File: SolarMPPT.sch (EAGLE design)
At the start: 33 parts, among them J1 CORTEX_DEBUG_SMD, U1 STM32F091CCT6, U3 LTC1155, U4 LM22674MRX-5.0, U5 3.3V

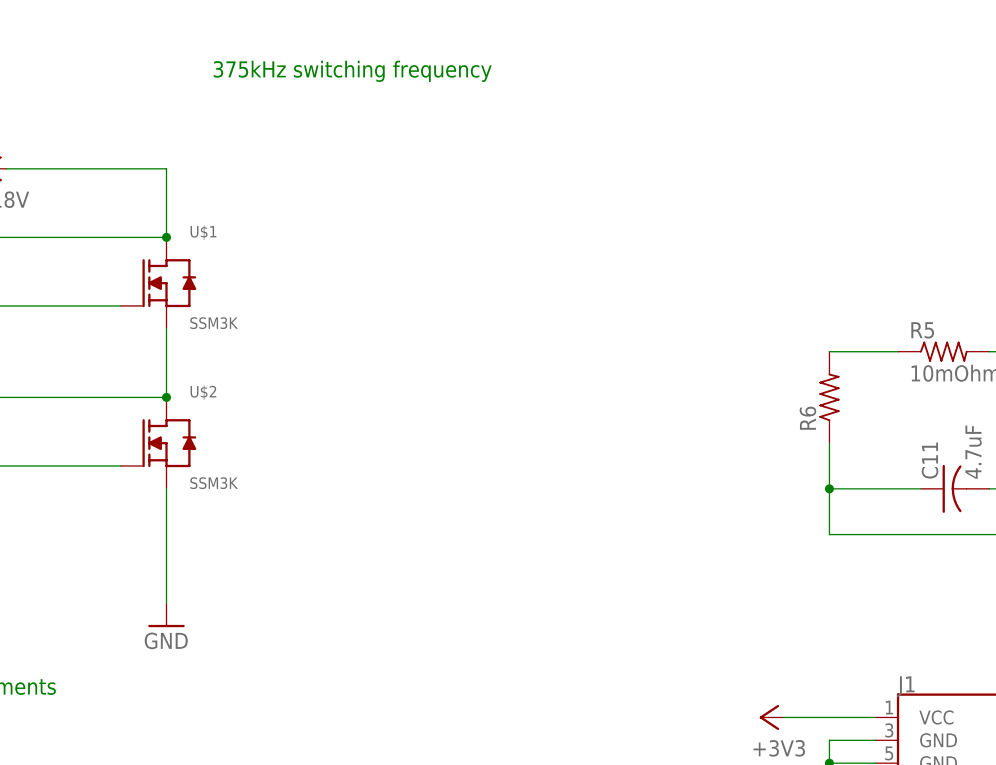
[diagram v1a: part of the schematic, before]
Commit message: finished Buck component selection
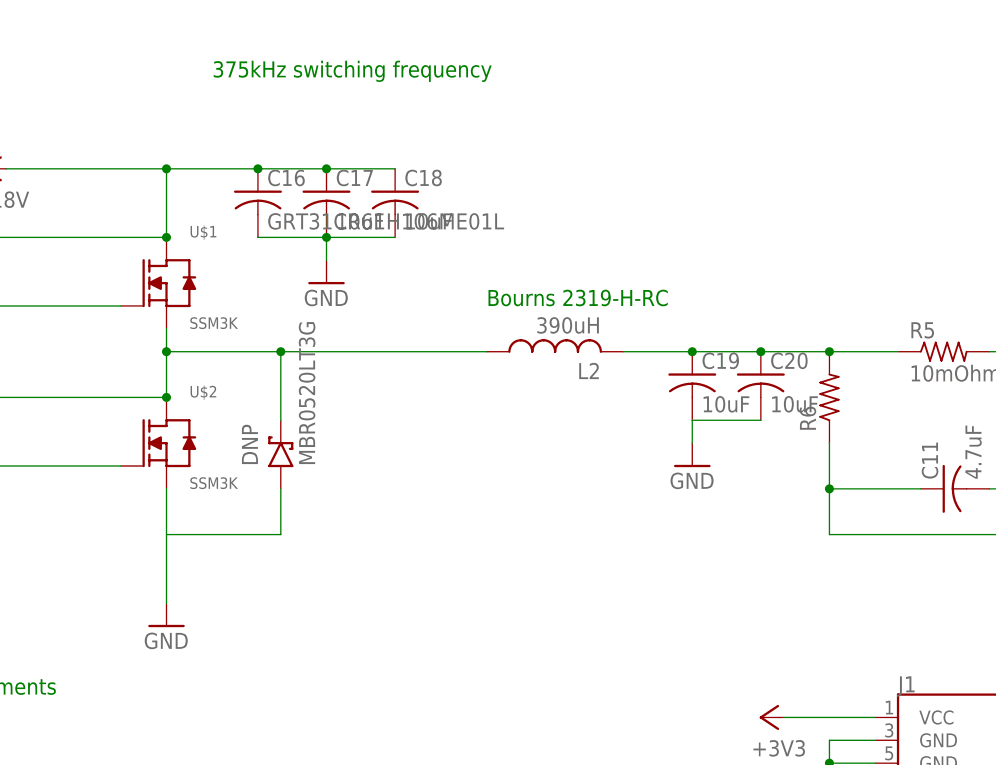
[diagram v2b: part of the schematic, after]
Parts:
- added C16: GRT31CR61H106ME01L, rcl:C-USC1206
- added C17, C18, C19, C20: 10uF, rcl:C-USC1206
- added DNP: MBR0520LT3G, FormE:MBR0520LT3G
- added L2: 390uH, rcl:L-USTJ6-U2
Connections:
- removed net N$3: R5.1, R6.2
- new net N$10: C19.1, C20.1, L2.2, R5.1, R6.2
- net +18V: now also C16.1, C17.1, C18.1
- net GND: now also C16.2, C17.2, C18.2, C19.2, C20.2, DNP.A
- net N$7: now also DNP.K, L2.1
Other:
- note added: "Bourns 2319-H-RC"
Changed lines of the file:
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@@
 <part name="GND16" library="supply1" library_urn="urn:adsk.eagle:library:371" deviceset="GND" device=""/>
 <part name="GND18" library="supply1" library_urn="urn:adsk.eagle:library:371" deviceset="GND" device=""/>
+<part name="C16" library="rcl" library_urn="urn:adsk.eagle:library:334" deviceset="C-US" device="C1206" package3d_urn="urn:adsk.eagle:package:23618/2" value="GRT31CR61H106ME01L"/>
+<part name="C17" library="rcl" library_urn="urn:adsk.eagle:library:334" deviceset="C-US" device="C1206" package3d_urn="urn:adsk.eagle:package:23618/2" value="10uF"/>
+<part name="C18" library="rcl" library_urn="urn:adsk.eagle:library:334" deviceset="C-US" device="C1206" package3d_urn="urn:adsk.eagle:package:23618/2" value="10uF"/>
+<part name="C19" library="rcl" library_urn="urn:adsk.eagle:library:334" deviceset="C-US" device="C1206" package3d_urn="urn:adsk.eagle:package:23618/2" value="10uF"/>
+<part name="C20" library="rcl" library_urn="urn:adsk.eagle:library:334" deviceset="C-US" device="C1206" package3d_urn="urn:adsk.eagle:package:23618/2" value="10uF"/>
+<part name="L2" library="rcl" library_urn="urn:adsk.eagle:library:334" deviceset="L-US" device="TJ6-U2" package3d_urn="urn:adsk.eagle:package:23510/1" value="390uH"/>
+<part name="GND19" library="supply1" library_urn="urn:adsk.eagle:library:371" deviceset="GND" device=""/>
+<part name="GND21" library="supply1" library_urn="urn:adsk.eagle:library:371" deviceset="GND" device=""/>
+<part name="DNP" library="FormE" deviceset="MBR0520LT3G" device="" value="MBR0520LT3G"/>
 </parts>
 <sheets>
@@
 <text x="-73.66" y="228.6" size="1.778" layer="97" rot="MR0">NC</text>
 <text x="-187.96" y="129.54" size="1.778" layer="91">Use LT1255 for higher voltage requirements</text>
+<text x="-91.44" y="172.72" size="1.778" layer="91">Bourns 2319-H-RC</text>
 </plain>
 <instances>
@@
 <instance part="GND18" gate="1" x="-203.2" y="147.32" smashed="yes">
 <attribute name="VALUE" x="-205.74" y="144.78" size="1.778" layer="96"/>
+</instance>
+<instance part="C16" gate="G$1" x="-116.84" y="185.42" smashed="yes">
+<attribute name="NAME" x="-115.824" y="186.055" size="1.778" layer="95"/>
+<attribute name="VALUE" x="-115.824" y="181.229" size="1.778" layer="96"/>
+</instance>
+<instance part="C17" gate="G$1" x="-109.22" y="185.42" smashed="yes">
+<attribute name="NAME" x="-108.204" y="186.055" size="1.778" layer="95"/>
+<attribute name="VALUE" x="-108.204" y="181.229" size="1.778" layer="96"/>
+</instance>
+<instance part="C18" gate="G$1" x="-101.6" y="185.42" smashed="yes">
+<attribute name="NAME" x="-100.584" y="186.055" size="1.778" layer="95"/>
+<attribute name="VALUE" x="-100.584" y="181.229" size="1.778" layer="96"/>
+</instance>
+<instance part="C19" gate="G$1" x="-68.58" y="165.1" smashed="yes">
+<attribute name="NAME" x="-67.564" y="165.735" size="1.778" layer="95"/>
+<attribute name="VALUE" x="-67.564" y="160.909" size="1.778" layer="96"/>
+</instance>
+<instance part="C20" gate="G$1" x="-60.96" y="165.1" smashed="yes">
+<attribute name="NAME" x="-59.944" y="165.735" size="1.778" layer="95"/>
+<attribute name="VALUE" x="-59.944" y="160.909" size="1.778" layer="96"/>
+</instance>
+<instance part="L2" gate="G$1" x="-83.82" y="167.64" smashed="yes" rot="R90">
+<attribute name="NAME" x="-78.74" y="166.37" size="1.778" layer="95" rot="R180"/>
+<attribute name="VALUE" x="-78.74" y="171.45" size="1.778" layer="96" rot="R180"/>
+</instance>
+<instance part="GND19" gate="1" x="-109.22" y="175.26" smashed="yes">
+<attribute name="VALUE" x="-111.76" y="172.72" size="1.778" layer="96"/>
+</instance>
+<instance part="GND21" gate="1" x="-68.58" y="154.94" smashed="yes">
+<attribute name="VALUE" x="-71.12" y="152.4" size="1.778" layer="96"/>
+</instance>
+<instance part="DNP" gate="G$1" x="-114.3" y="157.48" smashed="yes" rot="R90">
+<attribute name="NAME" x="-116.84" y="154.94" size="1.778" layer="95" rot="R90"/>
+<attribute name="VALUE" x="-110.49" y="154.94" size="1.778" layer="96" rot="R90"/>
 </instance>
 </instances>
@@
 <pinref part="U$2" gate="G$1" pin="S"/>
 <pinref part="GND16" gate="1" pin="GND"/>
-<wire x1="-127" y1="152.4" x2="-127" y2="139.7" width="0.1524" layer="91"/>
+<wire x1="-127" y1="152.4" x2="-127" y2="147.32" width="0.1524" layer="91"/>
+<wire x1="-127" y1="147.32" x2="-127" y2="139.7" width="0.1524" layer="91"/>
+<wire x1="-127" y1="147.32" x2="-114.3" y2="147.32" width="0.1524" layer="91"/>
+<pinref part="DNP" gate="G$1" pin="A"/>
+<wire x1="-114.3" y1="147.32" x2="-114.3" y2="152.4" width="0.1524" layer="91"/>
 </segment>
 <segment>
 <pinref part="U3" gate="P" pin="GND"/>
 <pinref part="GND18" gate="1" pin="GND"/>
+</segment>
+<segment>
+<pinref part="C19" gate="G$1" pin="2"/>
+<pinref part="GND21" gate="1" pin="GND"/>
+<pinref part="C20" gate="G$1" pin="2"/>
+<wire x1="-68.58" y1="160.02" x2="-68.58" y2="157.48" width="0.1524" layer="91"/>
+<wire x1="-68.58" y1="160.02" x2="-60.96" y2="160.02" width="0.1524" layer="91"/>
+</segment>
+<segment>
+<pinref part="C16" gate="G$1" pin="2"/>
+<pinref part="C17" gate="G$1" pin="2"/>
+<wire x1="-116.84" y1="180.34" x2="-109.22" y2="180.34" width="0.1524" layer="91"/>
+<pinref part="C18" gate="G$1" pin="2"/>
+<wire x1="-109.22" y1="180.34" x2="-101.6" y2="180.34" width="0.1524" layer="91"/>
+<junction x="-109.22" y="180.34"/>
+<pinref part="GND19" gate="1" pin="GND"/>
+<wire x1="-109.22" y1="177.8" x2="-109.22" y2="180.34" width="0.1524" layer="91"/>
 </segment>
 </net>
@@
 <wire x1="-203.2" y1="180.34" x2="-172.72" y2="180.34" width="0.1524" layer="91"/>
 <junction x="-172.72" y="180.34"/>
+<pinref part="C16" gate="G$1" pin="1"/>
+<wire x1="-127" y1="187.96" x2="-116.84" y2="187.96" width="0.1524" layer="91"/>
+<junction x="-127" y="187.96"/>
+<pinref part="C17" gate="G$1" pin="1"/>
+<wire x1="-116.84" y1="187.96" x2="-109.22" y2="187.96" width="0.1524" layer="91"/>
+<junction x="-116.84" y="187.96"/>
+<pinref part="C18" gate="G$1" pin="1"/>
+<wire x1="-109.22" y1="187.96" x2="-101.6" y2="187.96" width="0.1524" layer="91"/>
+<junction x="-109.22" y="187.96"/>
 </segment>
 </net>
@@
 <wire x1="33.02" y1="30.48" x2="33.02" y2="17.78" width="0.1524" layer="91"/>
 <label x="33.02" y="17.78" size="1.778" layer="95" rot="R90"/>
-</segment>
-</net>
-<net name="N$3" class="0">
-<segment>
-<pinref part="R6" gate="G$1" pin="2"/>
-<pinref part="R5" gate="G$1" pin="1"/>
-<wire x1="-53.34" y1="167.64" x2="-45.72" y2="167.64" width="0.1524" layer="91"/>
 </segment>
 </net>
@@
 <pinref part="U$1" gate="G$1" pin="S"/>
 <pinref part="U$2" gate="G$1" pin="D"/>
-<wire x1="-127" y1="170.18" x2="-127" y2="162.56" width="0.1524" layer="91"/>
+<wire x1="-127" y1="170.18" x2="-127" y2="167.64" width="0.1524" layer="91"/>
 <pinref part="U3" gate="B" pin="D"/>
+<wire x1="-127" y1="167.64" x2="-127" y2="162.56" width="0.1524" layer="91"/>
 <wire x1="-172.72" y1="157.48" x2="-172.72" y2="162.56" width="0.1524" layer="91"/>
 <wire x1="-172.72" y1="162.56" x2="-127" y2="162.56" width="0.1524" layer="91"/>
 <junction x="-127" y="162.56"/>
+<pinref part="L2" gate="G$1" pin="1"/>
+<wire x1="-127" y1="167.64" x2="-114.3" y2="167.64" width="0.1524" layer="91"/>
+<junction x="-127" y="167.64"/>
+<pinref part="DNP" gate="G$1" pin="K"/>
+<wire x1="-114.3" y1="167.64" x2="-91.44" y2="167.64" width="0.1524" layer="91"/>
+<wire x1="-114.3" y1="160.02" x2="-114.3" y2="167.64" width="0.1524" layer="91"/>
+<junction x="-114.3" y="167.64"/>
 </segment>
 </net>
@@
 </segment>
 </net>
+<net name="N$10" class="0">
+<segment>
+<pinref part="L2" gate="G$1" pin="2"/>
+<pinref part="C19" gate="G$1" pin="1"/>
+<wire x1="-76.2" y1="167.64" x2="-68.58" y2="167.64" width="0.1524" layer="91"/>
+<pinref part="C20" gate="G$1" pin="1"/>
+<wire x1="-68.58" y1="167.64" x2="-60.96" y2="167.64" width="0.1524" layer="91"/>
+<junction x="-68.58" y="167.64"/>
+<pinref part="R6" gate="G$1" pin="2"/>
+<pinref part="R5" gate="G$1" pin="1"/>
+<wire x1="-53.34" y1="167.64" x2="-45.72" y2="167.64" width="0.1524" layer="91"/>
+<wire x1="-60.96" y1="167.64" x2="-53.34" y2="167.64" width="0.1524" layer="91"/>
+<junction x="-60.96" y="167.64"/>
+<junction x="-53.34" y="167.64"/>
+</segment>
+</net>
